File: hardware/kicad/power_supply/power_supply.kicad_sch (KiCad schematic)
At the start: 34 parts, among them J1 PINHD_1x4_Female, J3 USB_C_Receptacle_PowerOnly_6P, Q1 AO3401A, U1 MT3608, U2 TP4056-42-ESOP8

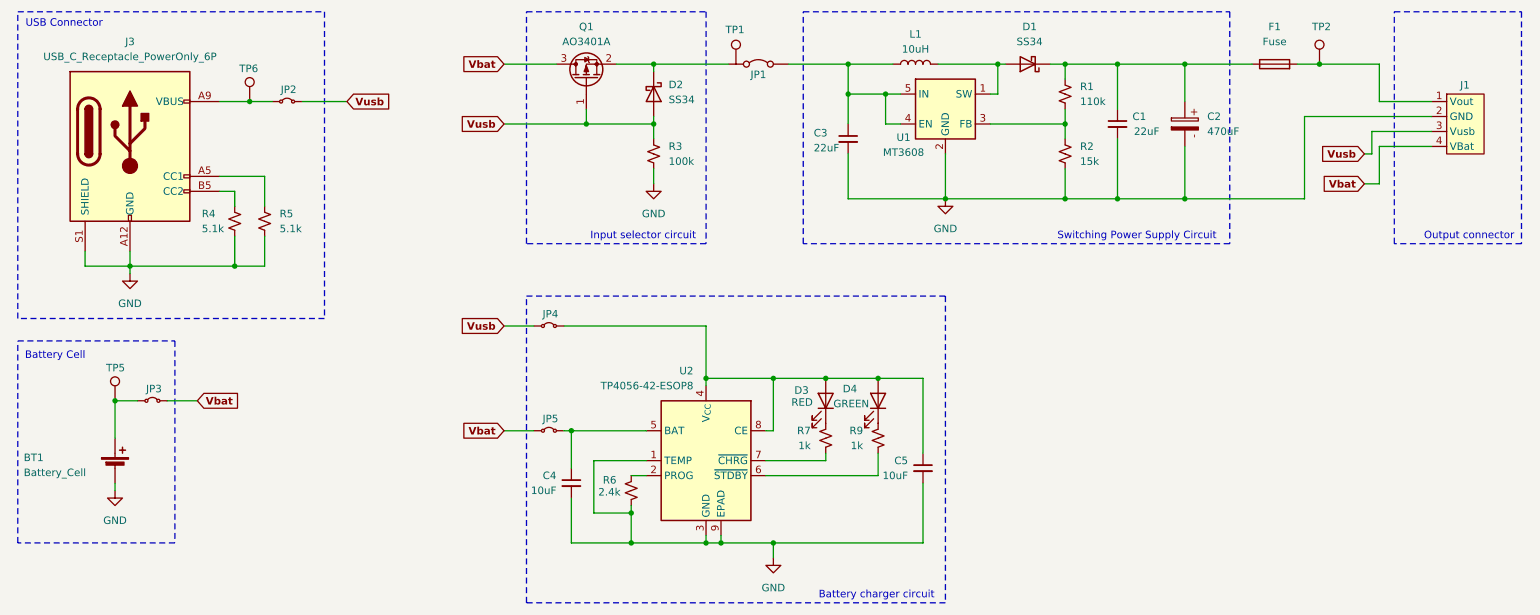
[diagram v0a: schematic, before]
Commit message: First draft completed for the power supply kicad project
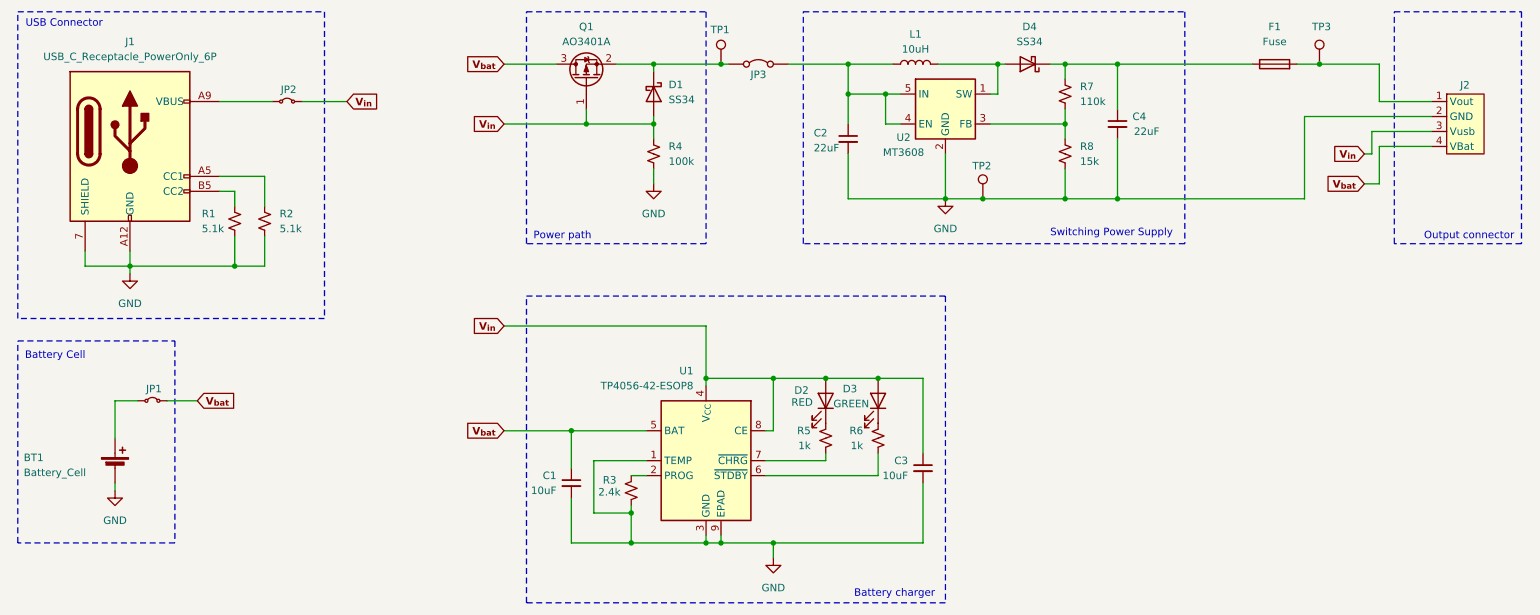
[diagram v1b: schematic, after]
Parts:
- removed C2: 470uF, Capacitor_THT:CP_Radial_D8.0mm_P3.50mm, symbol Power_Supply:470uF_16V
- removed JP4, JP5: Jumper_2_Small_Bridged, Connector_PinHeader_2.54mm:PinHeader_1x02_P2.54mm_Vertical, symbol Power_Supply:Jumper_2_Small_Bridged
- removed TP5, TP6: TestPoint, Connector_Pin:Pin_D1.0mm_L10.0mm, symbol Power_Supply:TestPoint
- added TP2: gnd, Connector_Pin:Pin_D1.3mm_L11.0mm, symbol Power_Supply:TestPoint
- F1: footprint Fuse:Fuse_BelFuse_0ZRE0075FF_L11.5mm_W4.8mm -> Fuse:Fuse_BelFuse_0ZRE0005FF_L8.3mm_W3.8mm
- J1: renamed from J3; LCSC (none) -> C456012
- J2: renamed from J1; footprint Connector_PinSocket_2.54mm:PinSocket_1x04_P2.54mm_Vertical -> Connector_Molex:Molex_KK-254_AE-6410-04A_1x04_P2.54mm_Vertical
- JP1: renamed from JP3; value Jumper_2_Small_Bridged -> Bat
- JP2: value Jumper_2_Small_Bridged -> usb
- JP3: renamed from JP1; value Jumper_2_Bridged -> power
- TP1: footprint Connector_Pin:Pin_D1.0mm_L10.0mm -> Connector_Pin:Pin_D1.3mm_L11.0mm
- TP3: renamed from TP2; value TestPoint -> out; footprint Connector_Pin:Pin_D1.0mm_L10.0mm -> Connector_Pin:Pin_D1.3mm_L11.0mm
- renumbered C4 to C1, C3 to C2, C5 to C3, C1 to C4, D2 to D1, D3 to D2, D4 to D3, D1 to D4, R4 to R1, R5 to R2, R6 to R3, R3 to R4, R7 to R5, R9 to R6, R1 to R7, R2 to R8, U2 to U1, U1 to U2
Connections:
- net Vbat is gone; now on net V_{bat}: J2.4 (VBat), JP1.2 (B), Q1.3 (D)
- net Vusb is gone; now on net V_{in}: D1.2 (A), J2.3 (Vusb), JP2.2 (B), Q1.1 (G), R4.1
- net GND: now also J1.7 (SHIELD), TP2.1; no longer J1.S1 (SHIELD)
- net at D1.1 (K), JP3.1 (A), Q1.2 (S): now also TP1.1
- net V_{bat}: now reaches C1.1, U1.5 (BAT)
- net V_{in}: now reaches C3.1, D2.2 (A), D3.2 (A), U1.4 (V_{CC}), U1.8 (CE)
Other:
- note added: "Battery charger"
- note added: "Power path"
- note added: "Switching Power Supply"
- note removed: "Battery charger circuit"
- note removed: "Input selector circuit"
- note removed: "Switching Power Supply Circuit"
- moved on the sheet: TP1

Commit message: Final version for power supply circuit
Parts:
- BT1: footprint Connector_JST:JST_EH_B2B-EH-A_1x02_P2.50mm_Vertical -> PowerSupply:JST_EH_B2B-EH-A_1x02_P2.50mm_Vertical
- C1, C3: footprint Capacitor_SMD:C_0402_1005Metric -> PowerSupply:C_0402_1005Metric
- C2, C4: footprint Capacitor_SMD:C_1206_3216Metric -> PowerSupply:C_1206_3216Metric
- D1, D4: footprint Diode_SMD:D_SMA -> PowerSupply:D_SMA
- D2, D3: footprint LED_SMD:LED_0805_2012Metric -> PowerSupply:LED_0805_2012Metric
- F1: footprint Fuse:Fuse_BelFuse_0ZRE0005FF_L8.3mm_W3.8mm -> PowerSupply:Fuse_BelFuse_0ZRE0005FF_L8.3mm_W3.8mm
- J1: footprint JLCPCB:TYPE-C-SMD_TYPE-C-6P -> PowerSupply:TYPE-C-SMD_TYPE-C-6P
- J2: footprint Connector_Molex:Molex_KK-254_AE-6410-04A_1x04_P2.54mm_Vertical -> PowerSupply:Molex_KK-254_AE-6410-04A_1x04_P2.54mm_Vertical
- JP1, JP2, JP3: footprint Connector_PinHeader_2.54mm:PinHeader_1x02_P2.54mm_Vertical -> PowerSupply:PinHeader_1x02_P2.54mm_Vertical
- L1: footprint JLCPCB:IND-SMD_2P-L5.0-W5.0 -> PowerSupply:IND-SMD_2P-L5.0-W5.0
- Q1: footprint Package_TO_SOT_SMD:SOT-23 -> PowerSupply:SOT-23
- R1, R2, R3, R4, R5, R6, R7, R8: footprint Resistor_SMD:R_0805_2012Metric -> PowerSupply:R_0805_2012Metric
- TP1, TP2, TP3: footprint Connector_Pin:Pin_D1.3mm_L11.0mm -> PowerSupply:Pin_D1.3mm_L11.0mm
- U1: footprint Package_SO:SOIC-8-1EP_3.9x4.9mm_P1.27mm_EP2.41x3.3mm_ThermalVias -> PowerSupply:SOIC-8-1EP_3.9x4.9mm_P1.27mm_EP2.41x3.3mm_ThermalVias
- U2: footprint Package_TO_SOT_SMD:TSOT-23-6_HandSoldering -> PowerSupply:TSOT-23-6_HandSoldering
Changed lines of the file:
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@@
 			)
 		)
-		(property "Footprint" "JLCPCB:IND-SMD_2P-L5.0-W5.0"
+		(property "Footprint" "PowerSupply:IND-SMD_2P-L5.0-W5.0"
 			(at 173.99 62.23 0)
 			(effects
@@
 			)
 		)
-		(property "Footprint" "Connector_PinHeader_2.54mm:PinHeader_1x02_P2.54mm_Vertical"
+		(property "Footprint" "PowerSupply:PinHeader_1x02_P2.54mm_Vertical"
 			(at 147.32 62.23 0)
 			(effects
@@
 			)
 		)
-		(property "Footprint" "Capacitor_SMD:C_0402_1005Metric"
+		(property "Footprint" "PowerSupply:C_0402_1005Metric"
 			(at 115.57 133.35 0)
 			(effects
@@
 			)
 		)
-		(property "Footprint" "Package_SO:SOIC-8-1EP_3.9x4.9mm_P1.27mm_EP2.41x3.3mm_ThermalVias"
+		(property "Footprint" "PowerSupply:SOIC-8-1EP_3.9x4.9mm_P1.27mm_EP2.41x3.3mm_ThermalVias"
 			(at 137.922 152.4 0)
 			(effects
@@
 			)
 		)
-		(property "Footprint" "Capacitor_SMD:C_1206_3216Metric"
+		(property "Footprint" "PowerSupply:C_1206_3216Metric"
 			(at 208.28 72.39 0)
 			(effects
@@
 			)
 		)
-		(property "Footprint" "Package_TO_SOT_SMD:SOT-23"
+		(property "Footprint" "PowerSupply:SOT-23"
 			(at 120.015 59.69 0)
 			(effects
@@
 			)
 		)
-		(property "Footprint" "Resistor_SMD:R_0805_2012Metric"
+		(property "Footprint" "PowerSupply:R_0805_2012Metric"
 			(at 125.73 134.62 0)
 			(effects
@@
 			)
 		)
-		(property "Footprint" "Diode_SMD:D_SMA"
+		(property "Footprint" "PowerSupply:D_SMA"
 			(at 125.095 67.31 0)
 			(effects
@@
 			)
 		)
-		(property "Footprint" "Connector_PinHeader_2.54mm:PinHeader_1x02_P2.54mm_Vertical"
+		(property "Footprint" "PowerSupply:PinHeader_1x02_P2.54mm_Vertical"
 			(at 44.45 119.38 0)
 			(effects
@@
 			)
 		)
-		(property "Footprint" "Connector_Pin:Pin_D1.3mm_L11.0mm"
+		(property "Footprint" "PowerSupply:Pin_D1.3mm_L11.0mm"
 			(at 247.65 62.23 0)
 			(effects
@@
 			)
 		)
-		(property "Footprint" "JLCPCB:TYPE-C-SMD_TYPE-C-6P"
+		(property "Footprint" "PowerSupply:TYPE-C-SMD_TYPE-C-6P"
 			(at 44.45 73.66 0)
 			(effects
@@
 			)
 		)
-		(property "Footprint" "Capacitor_SMD:C_1206_3216Metric"
+		(property "Footprint" "PowerSupply:C_1206_3216Metric"
 			(at 162.56 74.93 0)
 			(effects
@@
 			)
 		)
-		(property "Footprint" "LED_SMD:LED_0805_2012Metric"
+		(property "Footprint" "PowerSupply:LED_0805_2012Metric"
 			(at 167.64 119.38 0)
 			(effects
@@
 			)
 		)
-		(property "Footprint" "Diode_SMD:D_SMA"
+		(property "Footprint" "PowerSupply:D_SMA"
 			(at 193.04 57.785 0)
 			(effects
@@
 			)
 		)
-		(property "Footprint" "Connector_Pin:Pin_D1.3mm_L11.0mm"
+		(property "Footprint" "PowerSupply:Pin_D1.3mm_L11.0mm"
 			(at 190.5 85.09 0)
 			(effects
@@
 			)
 		)
-		(property "Footprint" "Resistor_SMD:R_0805_2012Metric"
+		(property "Footprint" "PowerSupply:R_0805_2012Metric"
 			(at 129.54 77.47 0)
 			(effects
@@
 			)
 		)
-		(property "Footprint" "Connector_JST:JST_EH_B2B-EH-A_1x02_P2.50mm_Vertical"
+		(property "Footprint" "PowerSupply:JST_EH_B2B-EH-A_1x02_P2.50mm_Vertical"
 			(at 38.1 129.286 90)
 			(effects
@@
 			)
 		)
-		(property "Footprint" "Fuse:Fuse_BelFuse_0ZRE0005FF_L8.3mm_W3.8mm"
+		(property "Footprint" "PowerSupply:Fuse_BelFuse_0ZRE0005FF_L8.3mm_W3.8mm"
 			(at 234.95 64.008 90)
 			(effects
@@
 			)
 		)
-		(property "Footprint" "Package_TO_SOT_SMD:TSOT-23-6_HandSoldering"
+		(property "Footprint" "PowerSupply:TSOT-23-6_HandSoldering"
 			(at 180.34 76.2 0)
 			(effects
@@
 			)
 		)
-		(property "Footprint" "Resistor_SMD:R_0805_2012Metric"
+		(property "Footprint" "PowerSupply:R_0805_2012Metric"
 			(at 58.42 88.9 0)
 			(effects
@@
 			)
 		)
-		(property "Footprint" "Connector_Molex:Molex_KK-254_AE-6410-04A_1x04_P2.54mm_Vertical"
+		(property "Footprint" "PowerSupply:Molex_KK-254_AE-6410-04A_1x04_P2.54mm_Vertical"
 			(at 267.97 59.69 0)
 			(effects
@@
 			)
 		)
-		(property "Footprint" "LED_SMD:LED_0805_2012Metric"
+		(property "Footprint" "PowerSupply:LED_0805_2012Metric"
 			(at 158.75 119.38 0)
 			(effects
@@
 			)
 		)
-		(property "Footprint" "Connector_Pin:Pin_D1.3mm_L11.0mm"
+		(property "Footprint" "PowerSupply:Pin_D1.3mm_L11.0mm"
 			(at 146.05 62.23 0)
 			(effects
@@
 			)
 		)
-		(property "Footprint" "Resistor_SMD:R_0805_2012Metric"
+		(property "Footprint" "PowerSupply:R_0805_2012Metric"
 			(at 167.64 125.73 0)
 			(effects
@@
 			)
 		)
-		(property "Footprint" "Resistor_SMD:R_0805_2012Metric"
+		(property "Footprint" "PowerSupply:R_0805_2012Metric"
 			(at 158.75 125.73 0)
 			(effects
@@
 			)
 		)
-		(property "Footprint" "Resistor_SMD:R_0805_2012Metric"
+		(property "Footprint" "PowerSupply:R_0805_2012Metric"
 			(at 199.39 67.31 0)
 			(effects
@@
 			)
 		)
-		(property "Footprint" "Resistor_SMD:R_0805_2012Metric"
+		(property "Footprint" "PowerSupply:R_0805_2012Metric"
 			(at 199.39 77.47 0)
 			(effects
@@
 			)
 		)
-		(property "Footprint" "Capacitor_SMD:C_0402_1005Metric"
+		(property "Footprint" "PowerSupply:C_0402_1005Metric"
 			(at 175.26 130.81 0)
 			(effects
@@
 			)
 		)
-		(property "Footprint" "Resistor_SMD:R_0805_2012Metric"
+		(property "Footprint" "PowerSupply:R_0805_2012Metric"
 			(at 63.5 88.9 0)
 			(effects
@@
 			)
 		)
-		(property "Footprint" "Connector_PinHeader_2.54mm:PinHeader_1x02_P2.54mm_Vertical"
+		(property "Footprint" "PowerSupply:PinHeader_1x02_P2.54mm_Vertical"
 			(at 67.31 68.58 0)
 			(effects
